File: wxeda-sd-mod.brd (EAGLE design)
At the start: 103.8 x 40.6 mm, 11 parts, among them U1 SD_CARD

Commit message: Added pull-up resistors
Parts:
- added R3, R4, R5, R6: 10k, SparkFun-Passives:AXIAL-0.3
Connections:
- net DSC: now also R4.P$2
- net DSD: now also R3.P$2
- net DSDP: now also R6.P$2
- net DSG: now also R5.P$2
- net VCC: now also R3.P$1, R4.P$1, R5.P$1, R6.P$1
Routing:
- net DSD: track 38.5 -> 67.7 mm
- net VCC: track 89.2 -> 101.9 mm
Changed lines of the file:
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@@
 <layer number="106" name="bPlate" color="7" fill="1" visible="no" active="yes"/>
 <layer number="107" name="Crop" color="7" fill="1" visible="no" active="yes"/>
+<layer number="108" name="fp8" color="7" fill="1" visible="no" active="yes"/>
+<layer number="109" name="fp9" color="7" fill="1" visible="no" active="yes"/>
+<layer number="110" name="fp0" color="7" fill="1" visible="no" active="yes"/>
+<layer number="111" name="LPC17xx" color="7" fill="1" visible="yes" active="yes"/>
+<layer number="112" name="tSilk" color="7" fill="1" visible="yes" active="yes"/>
 <layer number="116" name="Patch_BOT" color="9" fill="4" visible="no" active="yes"/>
 <layer number="121" name="_tsilk" color="7" fill="1" visible="no" active="yes"/>
 <layer number="122" name="_bsilk" color="7" fill="1" visible="no" active="yes"/>
+<layer number="123" name="tTestmark" color="7" fill="1" visible="no" active="yes"/>
+<layer number="124" name="bTestmark" color="7" fill="1" visible="no" active="yes"/>
 <layer number="125" name="_tNames" color="7" fill="1" visible="no" active="yes"/>
+<layer number="126" name="_bNames" color="7" fill="1" visible="yes" active="yes"/>
+<layer number="127" name="_tValues" color="7" fill="1" visible="yes" active="yes"/>
+<layer number="128" name="_bValues" color="7" fill="1" visible="yes" active="yes"/>
+<layer number="131" name="tAdjust" color="7" fill="1" visible="no" active="yes"/>
+<layer number="132" name="bAdjust" color="7" fill="1" visible="no" active="yes"/>
 <layer number="144" name="Drill_legend" color="7" fill="1" visible="no" active="yes"/>
 <layer number="151" name="HeatSink" color="7" fill="1" visible="no" active="yes"/>
+<layer number="152" name="_bDocu" color="7" fill="1" visible="yes" active="yes"/>
 <layer number="199" name="Contour" color="7" fill="1" visible="yes" active="yes"/>
 <layer number="200" name="200bmp" color="1" fill="10" visible="no" active="yes"/>
@@
 <layer number="223" name="223bmp" color="24" fill="1" visible="no" active="no"/>
 <layer number="224" name="224bmp" color="25" fill="1" visible="no" active="no"/>
+<layer number="248" name="Housing" color="7" fill="1" visible="yes" active="yes"/>
+<layer number="249" name="Edge" color="7" fill="1" visible="yes" active="yes"/>
 <layer number="250" name="Descript" color="3" fill="1" visible="no" active="no"/>
 <layer number="251" name="SMDround" color="12" fill="11" visible="no" active="no"/>
@@
 <attribute name="VALUE" x="20.447" y="4.064" size="0.6096" layer="27"/>
 </element>
+<element name="R3" library="SparkFun-Passives" package="AXIAL-0.3" value="10k" x="55.88" y="24.13" rot="R180"/>
+<element name="R4" library="SparkFun-Passives" package="AXIAL-0.3" value="10k" x="50.8" y="16.51" rot="R180"/>
+<element name="R5" library="SparkFun-Passives" package="AXIAL-0.3" value="10k" x="53.34" y="20.32" rot="R180"/>
+<element name="R6" library="SparkFun-Passives" package="AXIAL-0.3" value="10k" x="48.26" y="12.7" rot="R180"/>
 </elements>
 <signals>
@@
 <wire x1="33.02" y1="16.51" x2="26.67" y2="16.51" width="1.016" layer="1"/>
 <wire x1="36.34" y1="32.58" x2="36.83" y2="32.58" width="0.6096" layer="1"/>
-<wire x1="36.83" y1="32.58" x2="38.1" y2="34.29" width="1.016" layer="1"/>
-<wire x1="38.1" y1="34.29" x2="55.88" y2="34.29" width="1.016" layer="1"/>
-<wire x1="55.88" y1="34.29" x2="55.88" y2="39.37" width="1.016" layer="1"/>
+<wire x1="36.83" y1="32.58" x2="38.1" y2="35.56" width="1.016" layer="1"/>
+<wire x1="38.1" y1="35.56" x2="55.88" y2="35.56" width="1.016" layer="1"/>
+<wire x1="55.88" y1="35.56" x2="55.88" y2="39.37" width="1.016" layer="1"/>
 <wire x1="55.88" y1="39.37" x2="77.47" y2="39.37" width="1.016" layer="1"/>
 <wire x1="77.47" y1="35.56" x2="77.47" y2="39.37" width="1.016" layer="1"/>
@@
 <wire x1="22.86" y1="6.35" x2="22.86" y2="5.08" width="0.8128" layer="1"/>
 <wire x1="22.86" y1="5.08" x2="58.42" y2="5.08" width="0.8128" layer="1"/>
-<wire x1="58.42" y1="5.08" x2="58.42" y2="35.56" width="0.8128" layer="1"/>
+<wire x1="58.42" y1="5.08" x2="58.42" y2="12.7" width="0.8128" layer="1"/>
+<wire x1="58.42" y1="12.7" x2="58.42" y2="16.51" width="0.8128" layer="1"/>
+<wire x1="58.42" y1="16.51" x2="58.42" y2="20.32" width="0.8128" layer="1"/>
+<wire x1="58.42" y1="20.32" x2="58.42" y2="24.13" width="0.8128" layer="1"/>
+<wire x1="58.42" y1="24.13" x2="58.42" y2="35.56" width="0.8128" layer="1"/>
 <wire x1="58.42" y1="35.56" x2="74.93" y2="35.56" width="0.8128" layer="1"/>
 <contactref element="C1" pad="1"/>
 <wire x1="21.72" y1="6.35" x2="22.86" y2="6.35" width="0.6096" layer="1"/>
+<contactref element="R3" pad="P$1"/>
+<contactref element="R4" pad="P$1"/>
+<contactref element="R5" pad="P$1"/>
+<contactref element="R6" pad="P$1"/>
+<wire x1="59.69" y1="24.13" x2="58.42" y2="24.13" width="0.6096" layer="1"/>
+<wire x1="57.15" y1="20.32" x2="58.42" y2="20.32" width="0.6096" layer="1"/>
+<wire x1="54.61" y1="16.51" x2="58.42" y2="16.51" width="0.6096" layer="1"/>
+<wire x1="52.07" y1="12.7" x2="58.42" y2="12.7" width="0.6096" layer="1"/>
 </signal>
 <signal name="DSE">
@@
 <wire x1="29.74" y1="10.43" x2="29.21" y2="9.16" width="0.6096" layer="1"/>
 <wire x1="29.21" y1="9.16" x2="29.21" y2="7.62" width="0.6096" layer="1"/>
+<contactref element="R3" pad="P$2"/>
+<wire x1="41.91" y1="30.48" x2="41.91" y2="33.02" width="0.6096" layer="1"/>
+<wire x1="41.91" y1="33.02" x2="55.88" y2="33.02" width="0.6096" layer="1"/>
+<wire x1="55.88" y1="33.02" x2="55.88" y2="24.13" width="0.6096" layer="1"/>
+<wire x1="55.88" y1="24.13" x2="52.07" y2="24.13" width="0.6096" layer="1"/>
 </signal>
 <signal name="DSDP">
 <contactref element="JP1" pad="3"/>
 <contactref element="R1" pad="P$1"/>
-<wire x1="44.45" y1="8.89" x2="44.45" y2="30.48" width="0.6096" layer="1"/>
+<wire x1="44.45" y1="8.89" x2="44.45" y2="11.43" width="0.6096" layer="1"/>
+<contactref element="R6" pad="P$2"/>
+<wire x1="44.45" y1="12.7" x2="44.45" y2="30.48" width="0.6096" layer="1"/>
+<wire x1="44.45" y1="12.7" x2="44.45" y2="11.43" width="0.6096" layer="1"/>
 </signal>
 <signal name="DSC">
 <contactref element="JP1" pad="4"/>
 <contactref element="U1" pad="5"/>
-<wire x1="46.99" y1="30.48" x2="46.99" y2="6.35" width="0.6096" layer="1"/>
+<wire x1="46.99" y1="30.48" x2="46.99" y2="17.78" width="0.6096" layer="1"/>
+<wire x1="46.99" y1="16.51" x2="46.99" y2="6.35" width="0.6096" layer="1"/>
 <wire x1="46.99" y1="6.35" x2="26.09" y2="6.35" width="0.6096" layer="1"/>
 <wire x1="26.09" y1="6.35" x2="24.82" y2="10.43" width="0.6096" layer="1"/>
+<contactref element="R4" pad="P$2"/>
+<wire x1="46.99" y1="16.51" x2="46.99" y2="17.78" width="0.6096" layer="1"/>
 </signal>
 <signal name="DSG">
 <contactref element="JP1" pad="5"/>
 <contactref element="R2" pad="P$1"/>
-<wire x1="49.53" y1="8.89" x2="49.53" y2="30.48" width="0.6096" layer="1"/>
+<wire x1="49.53" y1="8.89" x2="49.53" y2="19.05" width="0.6096" layer="1"/>
+<contactref element="R5" pad="P$2"/>
+<wire x1="49.53" y1="20.32" x2="49.53" y2="30.48" width="0.6096" layer="1"/>
+<wire x1="49.53" y1="20.32" x2="49.53" y2="19.05" width="0.6096" layer="1"/>
 </signal>
 <signal name="DSEN4">

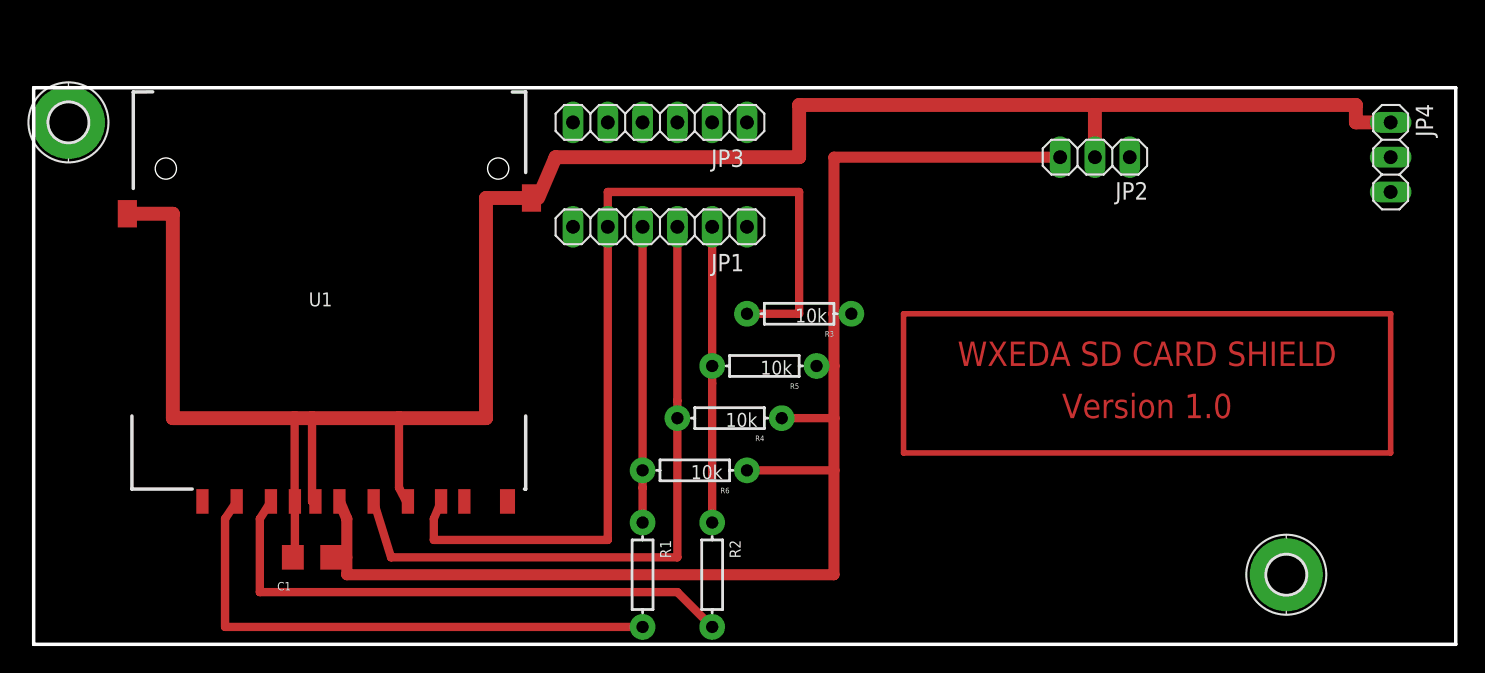
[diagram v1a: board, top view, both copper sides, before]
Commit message: Added tape in/out and tv out
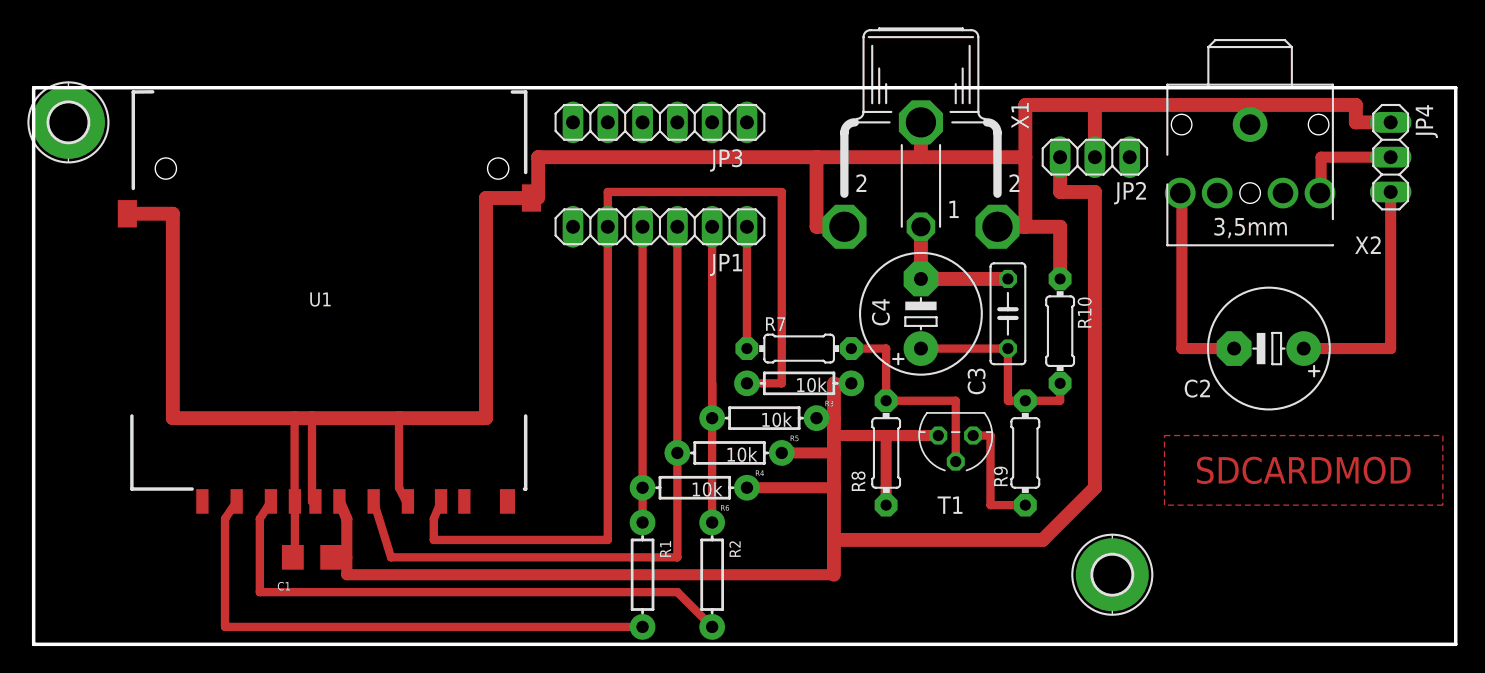
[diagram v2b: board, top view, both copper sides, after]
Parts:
- added C2: 10uF, adafruit:E5-8,5
- added C3: 22n, adafruit:C050-025X075
- added C4: 47uF, adafruit:E5-8,5
- added R10: 150, adafruit:0204/7
- added R7: 680, adafruit:0204/7
- added R8: 1k, adafruit:0204/7
- added R9: 51, adafruit:0204/7
- added T1: 2N3904, transistor:TO92
- added X1: TV OUT, con-hirschmann:TOBU3
- added X2: TAPE IN / OUT, adafruit:STX3100
- moved H3 12.7 mm to (78.7, 5.08)
- moved R3 5.08 mm to (55.9, 19.1)
- moved R5 3.81 mm to (53.3, 16.5)
- moved R4 2.54 mm to (50.8, 14.0)
- moved R6 1.27 mm to (48.3, 11.4)
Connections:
- new net N$2: R7.2, R8.1, T1.2
- new net N$4: C2.-, X2.5
- new net N$7: R9.1, T1.3
- new net N$8: C3.1, C4.+, R10.2, R9.2
- new net TVOUT: C3.2, C4.-, X1.1
- net A_IN: now also X2.2
- net DSEN4: now also R7.1
- net GND: now also R10.1, X1.2, X1.2@1, X1.2@2, X2.1
- net GREEN: now also C2.+
- net VCC: now also R8.2, T1.1
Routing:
- net N$2: track 91.4 -> 15.9 mm
- net VCC: track 101.9 -> 128.8 mm
- net GND: track 157.5 -> 183.2 mm
- net GREEN: track 0.00 -> 17.8 mm
- net N$4: track 0.00 -> 15.3 mm
- net N$8: track 0.00 -> 15.2 mm
- net TVOUT: track 0.00 -> 10.2 mm
- net N$7: track 0.00 -> 8.89 mm
- net DSEN4: track 0.00 -> 8.89 mm
- net A_IN: track 0.00 -> 7.78 mm
- net DSG: track 21.6 -> 24.1 mm
- net DSD: track 67.7 -> 70.2 mm
- added copper zone on layer 1, net N$5
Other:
- board text added: "SDCARDMOD"
- board text removed: "Version 1.0"
- board text removed: "WXEDA SD CARD SHIELD"

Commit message: small improvements
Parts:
- added C5: 10uF, adafruit:E5-8,5
- moved C2 4.02 mm to (86.4, 20.3)
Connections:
- new net N$6: C5.-, X2.2
- net A_IN: now also C5.+; no longer X2.2
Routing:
- net GREEN: track 17.8 -> 35.6 mm
- net N$6: track 0.00 -> 12.7 mm
- net A_IN: track 7.78 -> 20.3 mm
- net N$4: track 15.3 -> 12.7 mm
- removed copper zone on layer 1, net N$5
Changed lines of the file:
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@@
 <dimension x1="0" y1="0" x2="0" y2="40.64" x3="-7.62" y3="20.32" textsize="1.778" layer="20"/>
 <dimension x1="0" y1="40.63" x2="104.14" y2="40.64" x3="52.069265625" y3="48.255" textsize="1.778" layer="20"/>
-<text x="92.71" y="12.7" size="1.9304" layer="1" rot="SR0" align="center">SDCARDMOD</text>
+<text x="92.71" y="5.08" size="1.9304" layer="1" rot="SR0" align="center">SDCARDMOD</text>
 </plain>
 <attributes>
@@
 <element name="R5" library="SparkFun-Passives" package="AXIAL-0.3" value="10k" x="53.34" y="16.51" rot="R180"/>
 <element name="R6" library="SparkFun-Passives" package="AXIAL-0.3" value="10k" x="48.26" y="11.43" rot="R180"/>
-<element name="C2" library="adafruit" package="E5-8,5" value="10uF" x="90.17" y="21.59" rot="R180"/>
+<element name="C2" library="adafruit" package="E5-8,5" value="10uF" x="86.36" y="20.32" rot="R180"/>
 <element name="T1" library="transistor" package="TO92" value="2N3904" x="67.31" y="15.24" smashed="yes" rot="R180">
 <attribute name="NAME" x="67.945" y="10.795" size="1.27" layer="25" ratio="10" rot="R180"/>
@@
 <attribute name="VALUE" x="84.99" y="26.59" size="1.27" layer="27" ratio="10"/>
 </element>
+<element name="C5" library="adafruit" package="E5-8,5" value="10uF" x="96.52" y="20.32" rot="R180"/>
 </elements>
 <signals>
@@
 <signal name="A_IN">
 <contactref element="JP4" pad="2"/>
-<contactref element="X2" pad="2"/>
-<wire x1="93.9" y1="32.94" x2="93.98" y2="32.94" width="0.6096" layer="1"/>
-<wire x1="93.98" y1="32.94" x2="93.98" y2="35.56" width="0.8128" layer="1"/>
-<wire x1="93.98" y1="35.56" x2="99.06" y2="35.56" width="0.8128" layer="1"/>
+<contactref element="C5" pad="+"/>
+<wire x1="99.06" y1="35.56" x2="96.52" y2="35.56" width="0.8128" layer="1"/>
+<wire x1="96.52" y1="35.56" x2="96.52" y2="22.86" width="0.8128" layer="1"/>
+<wire x1="96.52" y1="22.86" x2="99.06" y2="22.86" width="0.8128" layer="1"/>
+<wire x1="99.06" y1="22.86" x2="99.06" y2="20.32" width="0.8128" layer="1"/>
 </signal>
 <signal name="GREEN">
 <contactref element="JP4" pad="3"/>
 <contactref element="C2" pad="+"/>
-<wire x1="99.06" y1="33.02" x2="99.06" y2="21.59" width="0.8128" layer="1"/>
-<wire x1="99.06" y1="21.59" x2="92.71" y2="21.59" width="0.8128" layer="1"/>
+<wire x1="88.9" y1="20.32" x2="88.9" y2="16.51" width="0.8128" layer="1"/>
+<wire x1="88.9" y1="16.51" x2="101.6" y2="16.51" width="0.8128" layer="1"/>
+<wire x1="101.6" y1="16.51" x2="101.6" y2="33.02" width="0.8128" layer="1"/>
+<wire x1="101.6" y1="33.02" x2="99.06" y2="33.02" width="0.8128" layer="1"/>
 </signal>
 <signal name="N$1">
@@
 <contactref element="C2" pad="-"/>
 <wire x1="83.7" y1="32.94" x2="83.82" y2="32.94" width="0.6096" layer="1"/>
-<wire x1="83.82" y1="32.94" x2="83.82" y2="21.59" width="0.8128" layer="1"/>
-<wire x1="83.82" y1="21.59" x2="87.63" y2="21.59" width="0.8128" layer="1"/>
-</signal>
-<signal name="N$5">
-<polygon width="1.016" layer="1" isolate="0.6096" thermals="no">
-<vertex x="82.55" y="15.24"/>
-<vertex x="102.87" y="15.24"/>
-<vertex x="102.87" y="10.16"/>
-<vertex x="82.55" y="10.16"/>
-</polygon>
+<wire x1="83.82" y1="32.94" x2="83.82" y2="20.32" width="0.8128" layer="1"/>
+</signal>
+<signal name="N$6">
+<contactref element="X2" pad="2"/>
+<contactref element="C5" pad="-"/>
+<wire x1="93.9" y1="32.94" x2="93.98" y2="32.94" width="0.8128" layer="1"/>
+<wire x1="93.98" y1="32.94" x2="93.98" y2="20.32" width="0.8128" layer="1"/>
 </signal>
 </signals>

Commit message: minor changes
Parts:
- H1, H3: value MOUNT-PAD-ROUND2.8 -> SEW_HOLE; device holes:2,8-PAD -> LilyPad-Wearables:SIMPLE_HOLE
- R10, R7, R8, R9: device adafruit:0204/7 -> SparkFun-Passives:AXIAL-0.3
- moved C2 3.59 mm to (83.8, 22.9)
- moved C5 3.59 mm to (94.0, 22.9)
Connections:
- net DSEN4: now also R7.P$1; no longer R7.1
- net GND: now also R10.P$1; no longer R10.1
- net N$2: now also R7.P$2, R8.P$1; no longer R7.2, R8.1
- net N$7: now also R9.P$1; no longer R9.1
- net N$8: now also R10.P$2, R9.P$2; no longer R10.2, R9.2
- net VCC: now also R8.P$2; no longer R8.2
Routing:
- net GREEN: track 35.6 -> 26.5 mm
- net A_IN: track 20.3 -> 15.2 mm
- net VCC: track 128.8 -> 125.9 mm
- net GND: track 183.2 -> 180.9 mm
- net N$4: track 12.7 -> 11.3 mm
- net N$7: track 8.89 -> 7.40 mm
- net N$6: track 12.7 -> 11.2 mm
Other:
- board size 103.8 x 40.6 mm -> 101.3 x 40.6 mm
